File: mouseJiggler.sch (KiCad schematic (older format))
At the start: 21 parts, among them J2 48037-0001, U1 ATmega16U2-MU, Y1 16MHz

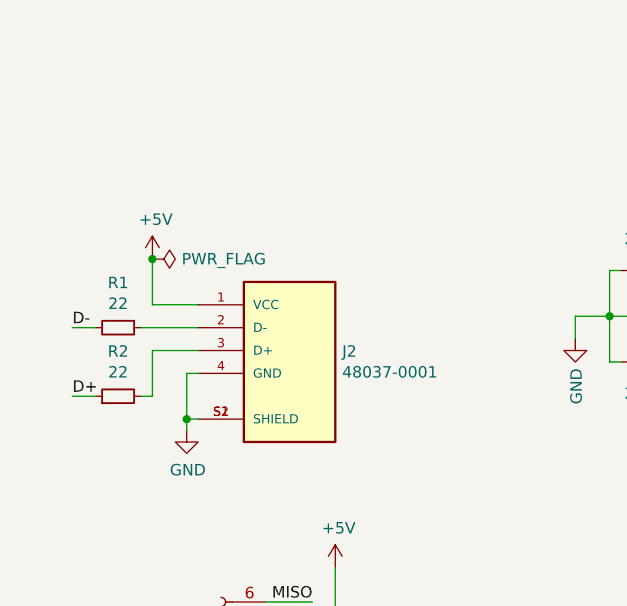
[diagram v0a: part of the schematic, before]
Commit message: Updated USB and silkscreen
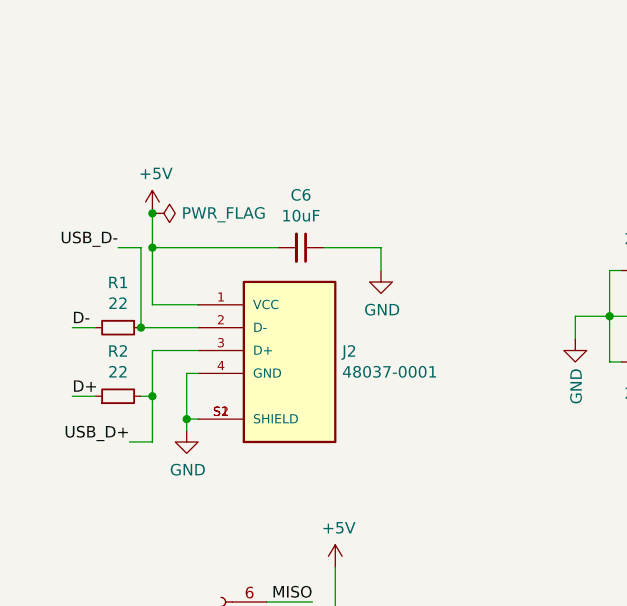
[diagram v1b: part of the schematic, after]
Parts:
- added C6: 10uF, Capacitor_SMD:C_0603_1608Metric, symbol Device:C_Small
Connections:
- net +5V: now also C6.2
- net GND: now also C6.1
- net USB_D-: now reaches J2.2 (D-), R1.1
- net USB_D+: now reaches J2.3 (D+), R2.2
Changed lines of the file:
@@
 L power:+5V #PWR01
 U 1 1 620975F9
-P 1900 2950
-F 0 "#PWR01" H 1900 2800 50  0001 C CNN
-F 1 "+5V" H 1915 3123 50  0000 C CNN
-F 2 "" H 1900 2950 50  0001 C CNN
-F 3 "" H 1900 2950 50  0001 C CNN
-	1    1900 2950
+P 1900 2750
+F 0 "#PWR01" H 1900 2600 50  0001 C CNN
+F 1 "+5V" H 1915 2923 50  0000 C CNN
+F 2 "" H 1900 2750 50  0001 C CNN
+F 3 "" H 1900 2750 50  0001 C CNN
+	1    1900 2750
 	1    0    0    -1
 $EndComp
@@
 L power:PWR_FLAG #FLG01
 U 1 1 61CA3313
-P 1900 2950
-F 0 "#FLG01" H 1900 3025 50  0001 C CNN
-F 1 "PWR_FLAG" V 1900 3078 50  0000 L CNN
-F 2 "" H 1900 2950 50  0001 C CNN
-F 3 "~" H 1900 2950 50  0001 C CNN
-	1    1900 2950
-	0    1    1    0
-$EndComp
-Connection ~ 1900 2950
+P 1900 2750
+F 0 "#FLG01" H 1900 2825 50  0001 C CNN
+F 1 "PWR_FLAG" V 1900 2878 50  0000 L CNN
+F 2 "" H 1900 2750 50  0001 C CNN
+F 3 "~" H 1900 2750 50  0001 C CNN
+	1    1900 2750
+	0    1    1    0
+$EndComp
 $Comp
 L SnapEDA:48037-0001 J2
@@
 $EndComp
 Wire Wire Line
-	2100 3150 1900 3150
-Wire Wire Line
-	1900 2950 1900 3150
-Wire Wire Line
 	1850 3250 2100 3250
 Wire Wire Line
@@
 $EndComp
 NoConn ~ 6650 4600
+$Comp
+L Device:C_Small C6
+U 1 1 61A95A6D
+P 2550 2900
+F 0 "C6" V 2321 2900 50  0000 C CNN
+F 1 "10uF" V 2412 2900 50  0000 C CNN
+F 2 "Capacitor_SMD:C_0603_1608Metric" H 2550 2900 50  0001 C CNN
+F 3 "~" H 2550 2900 50  0001 C CNN
+	1    2550 2900
+	0    1    1    0
+$EndComp
+Wire Wire Line
+	2100 3150 1900 3150
+Wire Wire Line
+	1900 3150 1900 2900
+Connection ~ 1900 2750
+Wire Wire Line
+	1900 2900 2450 2900
+Connection ~ 1900 2900
+Wire Wire Line
+	1900 2900 1900 2750
+Wire Wire Line
+	2650 2900 2900 2900
+Wire Wire Line
+	2900 2900 2900 3000
+$Comp
+L power:GND #PWR012
+U 1 1 61AAFA5A
+P 2900 3000
+F 0 "#PWR012" H 2900 2750 50  0001 C CNN
+F 1 "GND" H 2905 2827 50  0000 C CNN
+F 2 "" H 2900 3000 50  0001 C CNN
+F 3 "" H 2900 3000 50  0001 C CNN
+	1    2900 3000
+	1    0    0    -1
+$EndComp
+Wire Wire Line
+	1900 3550 1900 3750
+Wire Wire Line
+	1900 3750 1800 3750
+Connection ~ 1900 3550
+Wire Wire Line
+	1850 3250 1850 2900
+Wire Wire Line
+	1850 2900 1750 2900
+Connection ~ 1850 3250
+Text Label 1800 3750 2    50   ~ 0
+USB_D+
+Text Label 1750 2900 2    50   ~ 0
+USB_D-
 $EndSCHEMATC
